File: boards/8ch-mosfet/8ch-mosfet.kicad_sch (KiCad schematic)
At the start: 14 parts, among them J1 N2K, J2 I2C, J3 Screw_Terminal_01x08, J4 Screw_Terminal_01x08, U1 ESP32-DEVKITC, U2 MCP3208, U3 R-78B3.3-2.0

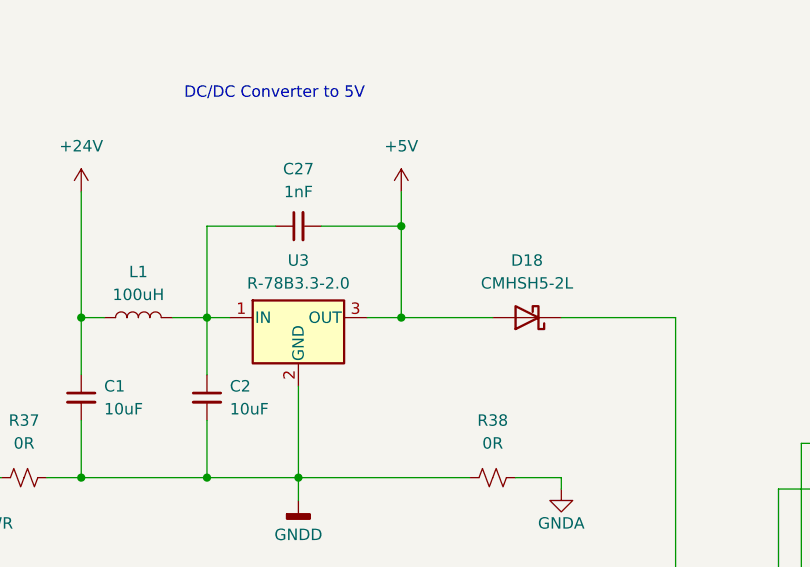
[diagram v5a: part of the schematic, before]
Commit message: changed the power input module
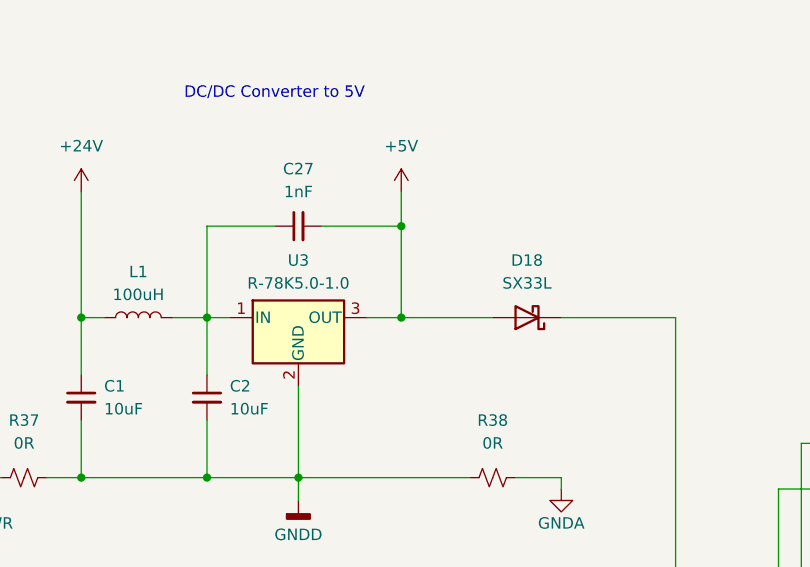
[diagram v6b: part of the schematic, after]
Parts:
- D18: value CMHSH5-2L -> SX33L; footprint Diode_SMD:D_SOD-323_HandSoldering -> Diode_SMD:D_SMA
- U3: value R-78B3.3-2.0 -> R-78K5.0-1.0
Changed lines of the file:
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@@
       (effects (font (size 1.27 1.27)))
     )
-    (property "Value" "R-78B3.3-2.0" (at 54.61 57.15 0)
+    (property "Value" "R-78K5.0-1.0 " (at 54.61 57.15 0)
       (effects (font (size 1.27 1.27)))
     )
@@
       (effects (font (size 1.27 1.27)))
     )
-    (property "Value" "CMHSH5-2L" (at 80.01 57.15 0)
-      (effects (font (size 1.27 1.27)))
-    )
-    (property "Footprint" "Diode_SMD:D_SOD-323_HandSoldering" (at 80.01 60.96 0)
-      (effects (font (size 1.27 1.27)) hide)
-    )
+    (property "Value" "SX33L" (at 80.01 57.15 0)
+      (effects (font (size 1.27 1.27)))
+    )
+    (property "Footprint" "Diode_SMD:D_SMA" (at 80.01 60.96 0)
+      (effects (font (size 1.27 1.27)) hide)
+    )

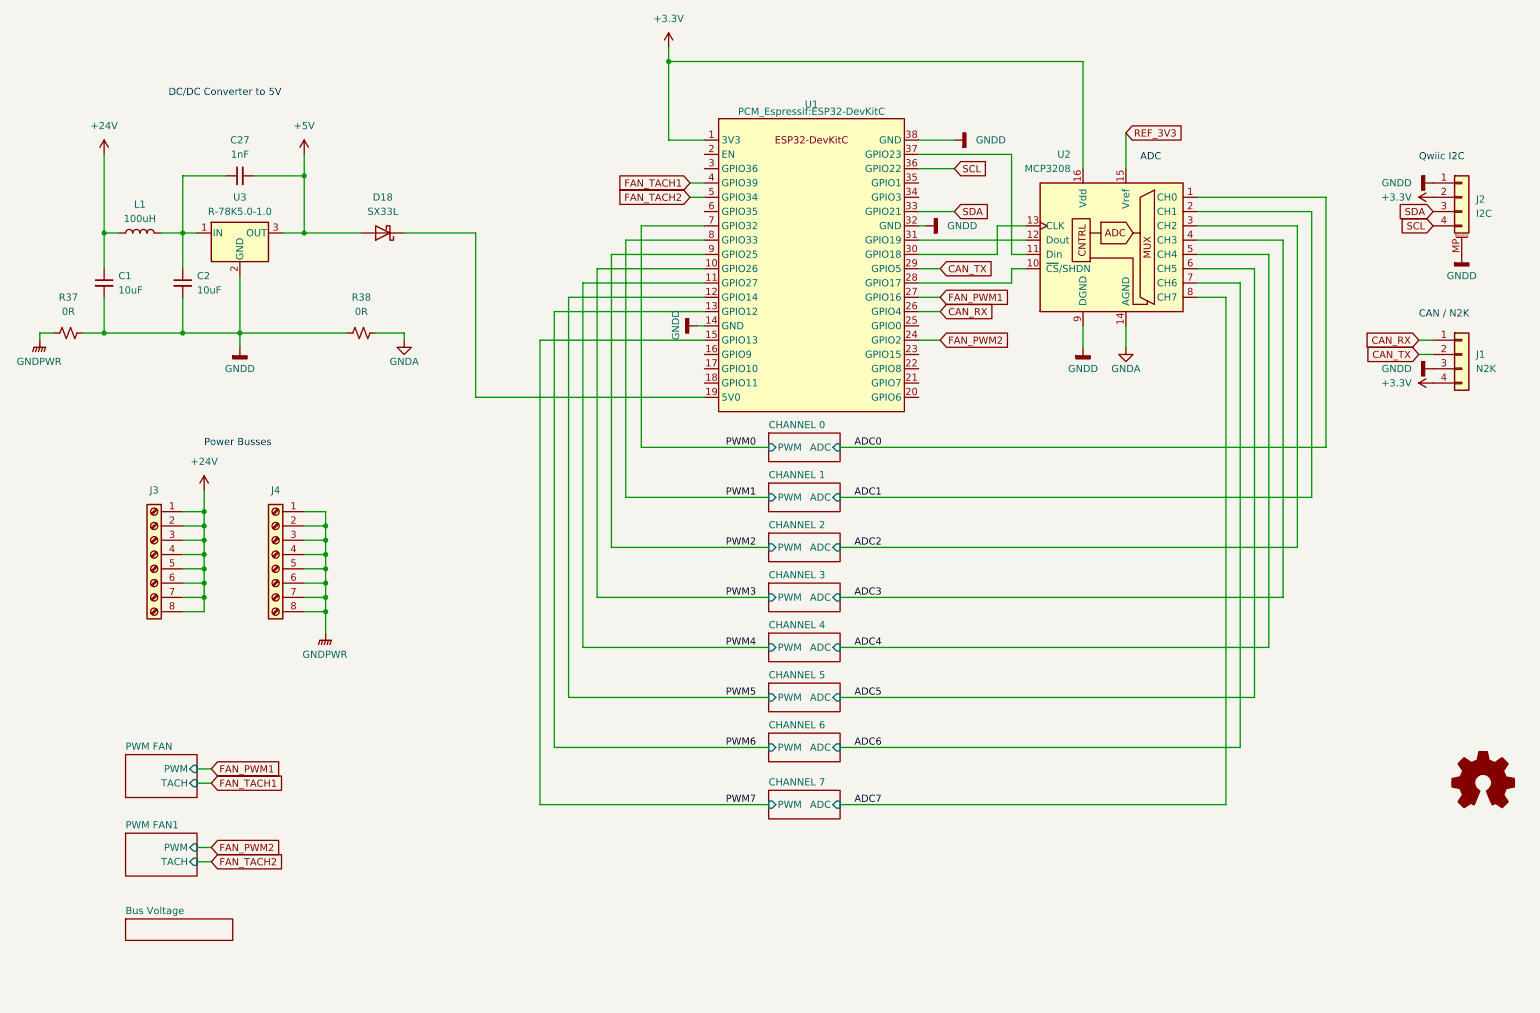
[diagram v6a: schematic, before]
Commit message: upgraded the i2c/serial connectors + power based on the sailor hat schematic
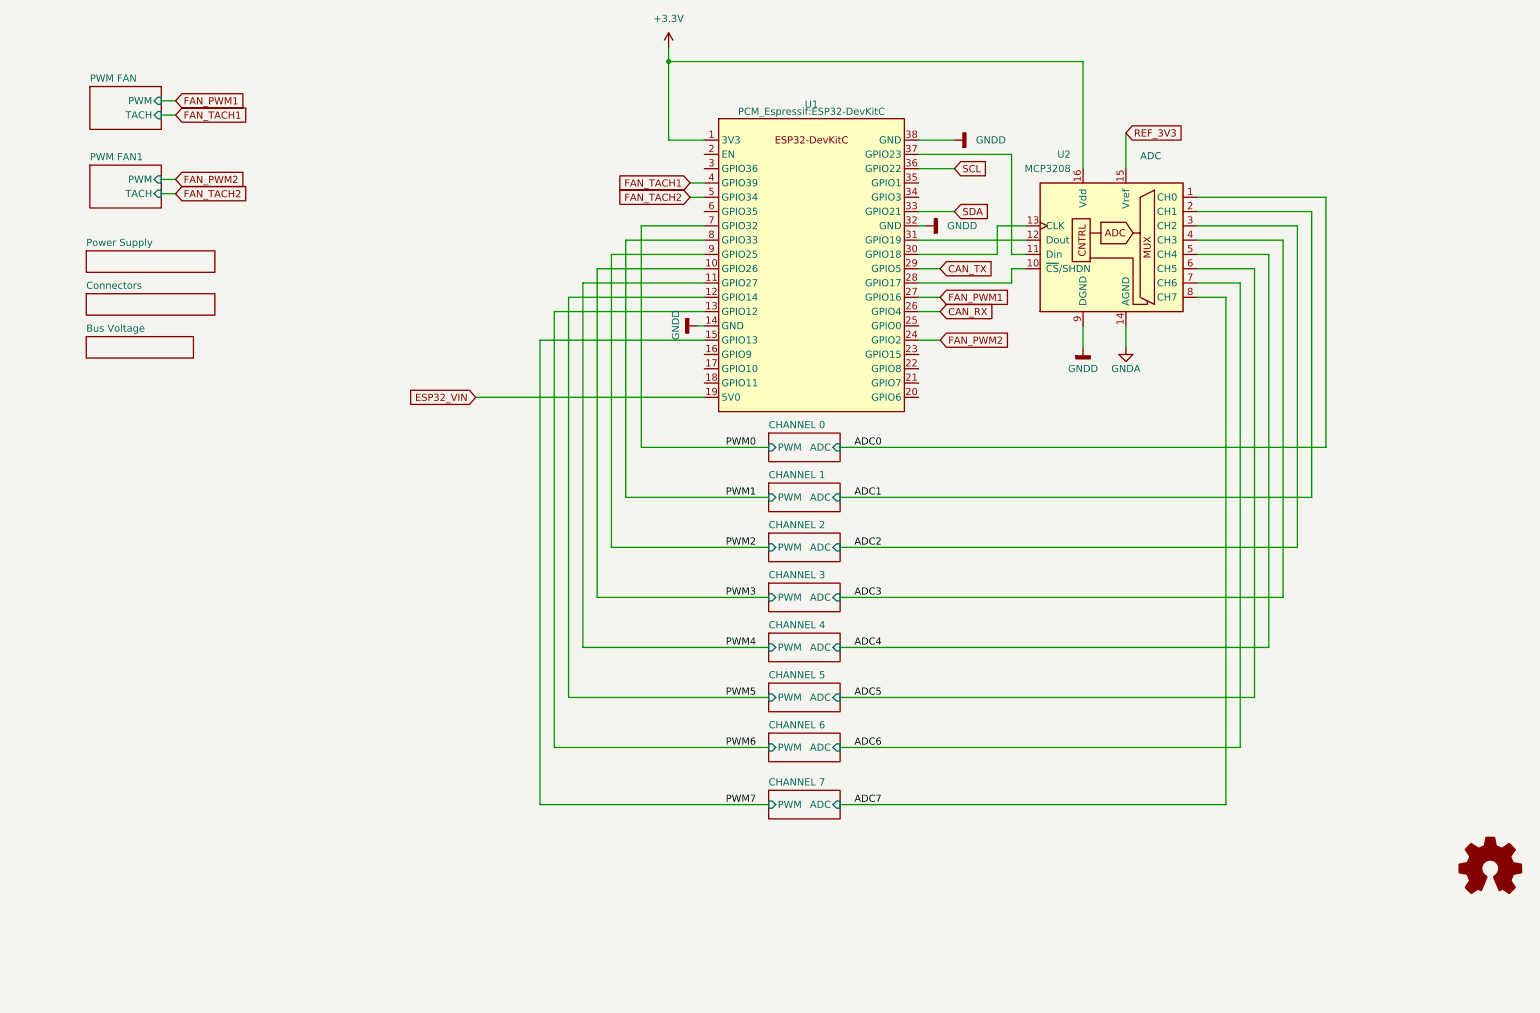
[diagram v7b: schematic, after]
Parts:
- removed C1, C2: 10uF, Capacitor_SMD:C_0805_2012Metric_Pad1.18x1.45mm_HandSolder, symbol Device:C_Small
- removed C27: 1nF, Capacitor_SMD:C_0805_2012Metric_Pad1.18x1.45mm_HandSolder, symbol Device:C_Small
- removed D18: SX33L, Diode_SMD:D_SMA, symbol Device:D_Schottky
- removed J1: N2K, Connector_PinSocket_2.54mm:PinSocket_1x04_P2.54mm_Horizontal, symbol Connector_Generic:Conn_01x04
- removed J2: I2C, Connector_JST:JST_SH_SM04B-SRSS-TB_1x04-1MP_P1.00mm_Horizontal, symbol Connector_Generic_MountingPin:Conn_01x04_MountingPin
- removed J3, J4: Screw_Terminal_01x08, gnarboard:Busbar 1x9 .375in, symbol Connector:Screw_Terminal_01x08
- removed L1: 100uH, Inductor_SMD:L_1210_3225Metric_Pad1.42x2.65mm_HandSolder, symbol Device:L
- removed R37, R38: 0R, Resistor_SMD:R_0805_2012Metric_Pad1.20x1.40mm_HandSolder, symbol Device:R_Small_US
- removed U3: R-78K5.0-1.0, gnarboard:RECOM R-78K, symbol Regulator_Switching:R-78B3.3-2.0
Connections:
- net ESP32_VIN: now reaches U1.19 (5V0)
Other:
- added sheet Connectors (connectors.kicad_sch)
- added sheet Power Supply (power.kicad_sch)
- note removed: "CAN / N2K"
- note removed: "DC/DC Converter to 5V"
- note removed: "Power Busses"
- note removed: "Qwiic I2C"

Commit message: silkscreen almost complete
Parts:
- added H1, H2, H3, H4, H5: MountingHole, MountingHole:MountingHole_3.2mm_M3_DIN965_Pad, symbol Mechanical:MountingHole
- U1: footprint PCM_Espressif:ESP32-DevKitC -> gnarboard:ESP32-DevKitC
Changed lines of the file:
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@@
-    )
-  )
-  (symbol (lib_id "Graphic:Logo_Open_Hardware_Small") (at 276.86 173.99 0) (unit 1)
-    (in_bom no) (on_board yes) (dnp no) (fields_autoplaced)
-    (property "Reference" "#SYM1" (at 276.86 167.005 0)
-      (effects (font (size 1.27 1.27)) hide)
-    )
-    (property "Value" "Logo_Open_Hardware_Small" (at 276.86 179.705 0)
-      (effects (font (size 1.27 1.27)) hide)
-    )
-    (property "Footprint" "Symbol:OSHW-Logo2_24.3x20mm_SilkScreen" (at 276.86 173.99 0)
-      (effects (font (size 1.27 1.27)) hide)
-    )
-    (property "Datasheet" "~" (at 276.86 173.99 0)
-      (effects (font (size 1.27 1.27)) hide)
-    )
-    (property "Sim.Enable" "0" (at 276.86 173.99 0)
-      (effects (font (size 1.27 1.27)) hide)
-    )
-    (instances
-      (project "8ch-mosfet"
-        (path "/c83c6236-96e9-46ad-9d7a-9e2efa4a7966"
-          (reference "#SYM1") (unit 1)
-        )
-      )
     )
   )
@@
     )
   )
+  (symbol (lib_id "Mechanical:MountingHole") (at 15.875 184.785 0) (unit 1)
+    (in_bom yes) (on_board yes) (dnp no) (fields_autoplaced)
+    (property "Reference" "H3" (at 18.415 183.515 0)
+      (effects (font (size 1.27 1.27)) (justify left))
+    )
+    (property "Value" "MountingHole" (at 18.415 186.055 0)
+      (effects (font (size 1.27 1.27)) (justify left))
+    )
+    (property "Footprint" "MountingHole:MountingHole_3.2mm_M3_DIN965_Pad" (at 15.875 184.785 0)
+      (effects (font (size 1.27 1.27)) hide)
+    )
+    (property "Datasheet" "~" (at 15.875 184.785 0)
+      (effects (font (size 1.27 1.27)) hide)
+    )
+    (instances
+      (project "8ch-mosfet"
+        (path "/c83c6236-96e9-46ad-9d7a-9e2efa4a7966"
+          (reference "H3") (unit 1)
+        )
+      )
+    )
+  )
   (symbol (lib_id "power:GNDA") (at 212.09 81.28 0) (unit 1)
     (in_bom yes) (on_board yes) (dnp no)
@@
         (path "/c83c6236-96e9-46ad-9d7a-9e2efa4a7966"
           (reference "#PWR02") (unit 1)
+        )
+      )
+    )
+  )
+  (symbol (lib_id "Mechanical:MountingHole") (at 15.875 194.945 0) (unit 1)
+    (in_bom yes) (on_board yes) (dnp no) (fields_autoplaced)
+    (property "Reference" "H5" (at 18.415 193.675 0)
+      (effects (font (size 1.27 1.27)) (justify left))
+    )
+    (property "Value" "MountingHole" (at 18.415 196.215 0)
+      (effects (font (size 1.27 1.27)) (justify left))
+    )
+    (property "Footprint" "MountingHole:MountingHole_3.2mm_M3_DIN965_Pad" (at 15.875 194.945 0)
+      (effects (font (size 1.27 1.27)) hide)
+    )
+    (property "Datasheet" "~" (at 15.875 194.945 0)
+      (effects (font (size 1.27 1.27)) hide)
+    )
+    (instances
+      (project "8ch-mosfet"
+        (path "/c83c6236-96e9-46ad-9d7a-9e2efa4a7966"
+          (reference "H5") (unit 1)
+        )
+      )
+    )
+  )
+  (symbol (lib_id "Mechanical:MountingHole") (at 15.875 179.705 0) (unit 1)
+    (in_bom yes) (on_board yes) (dnp no) (fields_autoplaced)
+    (property "Reference" "H2" (at 18.415 178.435 0)
+      (effects (font (size 1.27 1.27)) (justify left))
+    )
+    (property "Value" "MountingHole" (at 18.415 180.975 0)
+      (effects (font (size 1.27 1.27)) (justify left))
+    )
+    (property "Footprint" "MountingHole:MountingHole_3.2mm_M3_DIN965_Pad" (at 15.875 179.705 0)
+      (effects (font (size 1.27 1.27)) hide)
+    )
+    (property "Datasheet" "~" (at 15.875 179.705 0)
+      (effects (font (size 1.27 1.27)) hide)
+    )
+    (instances
+      (project "8ch-mosfet"
+        (path "/c83c6236-96e9-46ad-9d7a-9e2efa4a7966"
+          (reference "H2") (unit 1)
         )
       )
@@
       (effects (font (size 1.27 1.27)) hide)
     )
-    (property "Footprint" "PCM_Espressif:ESP32-DevKitC" (at 156.21 39.37 0)
+    (property "Footprint" "gnarboard:ESP32-DevKitC" (at 156.21 39.37 0)
       (effects (font (size 1.27 1.27)))
     )
@@
     )
   )
+  (symbol (lib_id "Mechanical:MountingHole") (at 15.875 174.625 0) (unit 1)
+    (in_bom yes) (on_board yes) (dnp no) (fields_autoplaced)
+    (property "Reference" "H1" (at 18.415 173.355 0)
+      (effects (font (size 1.27 1.27)) (justify left))
+    )
+    (property "Value" "MountingHole" (at 18.415 175.895 0)
+      (effects (font (size 1.27 1.27)) (justify left))
+    )
+    (property "Footprint" "MountingHole:MountingHole_3.2mm_M3_DIN965_Pad" (at 15.875 174.625 0)
+      (effects (font (size 1.27 1.27)) hide)
+    )
+    (property "Datasheet" "~" (at 15.875 174.625 0)
+      (effects (font (size 1.27 1.27)) hide)
+    )
+    (instances
+      (project "8ch-mosfet"
+        (path "/c83c6236-96e9-46ad-9d7a-9e2efa4a7966"
+          (reference "H1") (unit 1)
+        )
+      )
+    )
+  )
   (symbol (lib_id "power:GNDD") (at 181.61 44.45 90) (unit 1)
     (in_bom yes) (on_board yes) (dnp no) (fields_autoplaced)
@@
         (path "/c83c6236-96e9-46ad-9d7a-9e2efa4a7966"
           (reference "#PWR03") (unit 1)
+        )
+      )
+    )
+  )
+  (symbol (lib_id "Mechanical:MountingHole") (at 15.875 189.865 0) (unit 1)
+    (in_bom yes) (on_board yes) (dnp no) (fields_autoplaced)
+    (property "Reference" "H4" (at 18.415 188.595 0)
+      (effects (font (size 1.27 1.27)) (justify left))
+    )
+    (property "Value" "MountingHole" (at 18.415 191.135 0)
+      (effects (font (size 1.27 1.27)) (justify left))
+    )
+    (property "Footprint" "MountingHole:MountingHole_3.2mm_M3_DIN965_Pad" (at 15.875 189.865 0)
+      (effects (font (size 1.27 1.27)) hide)
+    )
+    (property "Datasheet" "~" (at 15.875 189.865 0)
+      (effects (font (size 1.27 1.27)) hide)
+    )
+    (instances
+      (project "8ch-mosfet"
+        (path "/c83c6236-96e9-46ad-9d7a-9e2efa4a7966"
+          (reference "H4") (unit 1)
         )
       )
@@
         )
       )
+    )
+  )
+  (symbol (lib_id "Graphic:Logo_Open_Hardware_Small") (at 278.13 174.625 0) (unit 1)
+    (in_bom no) (on_board no) (dnp no) (fields_autoplaced)
+    (property "Reference" "#SYM1" (at 278.13 167.64 0)
+      (effects (font (size 1.27 1.27)) hide)
+    )
+    (property "Value" "Logo_Open_Hardware_Small" (at 278.13 180.34 0)
+      (effects (font (size 1.27 1.27)) hide)
+    )
+    (property "Footprint" "Symbol:OSHW-Logo2_14.6x12mm_SilkScreen" (at 278.13 174.625 0)
+      (effects (font (size 1.27 1.27)) hide)
+    )
+    (property "Datasheet" "~" (at 278.13 174.625 0)
+      (effects (font (size 1.27 1.27)) hide)
+    )
+    (property "Sim.Enable" "0" (at 278.13 174.625 0)
+      (effects (font (size 1.27 1.27)) hide)
+    )
+    (instances
+      (project "8ch-mosfet"
+        (path "/c83c6236-96e9-46ad-9d7a-9e2efa4a7966"
+          (reference "#SYM1") (unit 1)
+        )
+      )
